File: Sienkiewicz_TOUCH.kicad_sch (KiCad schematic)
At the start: 0 parts

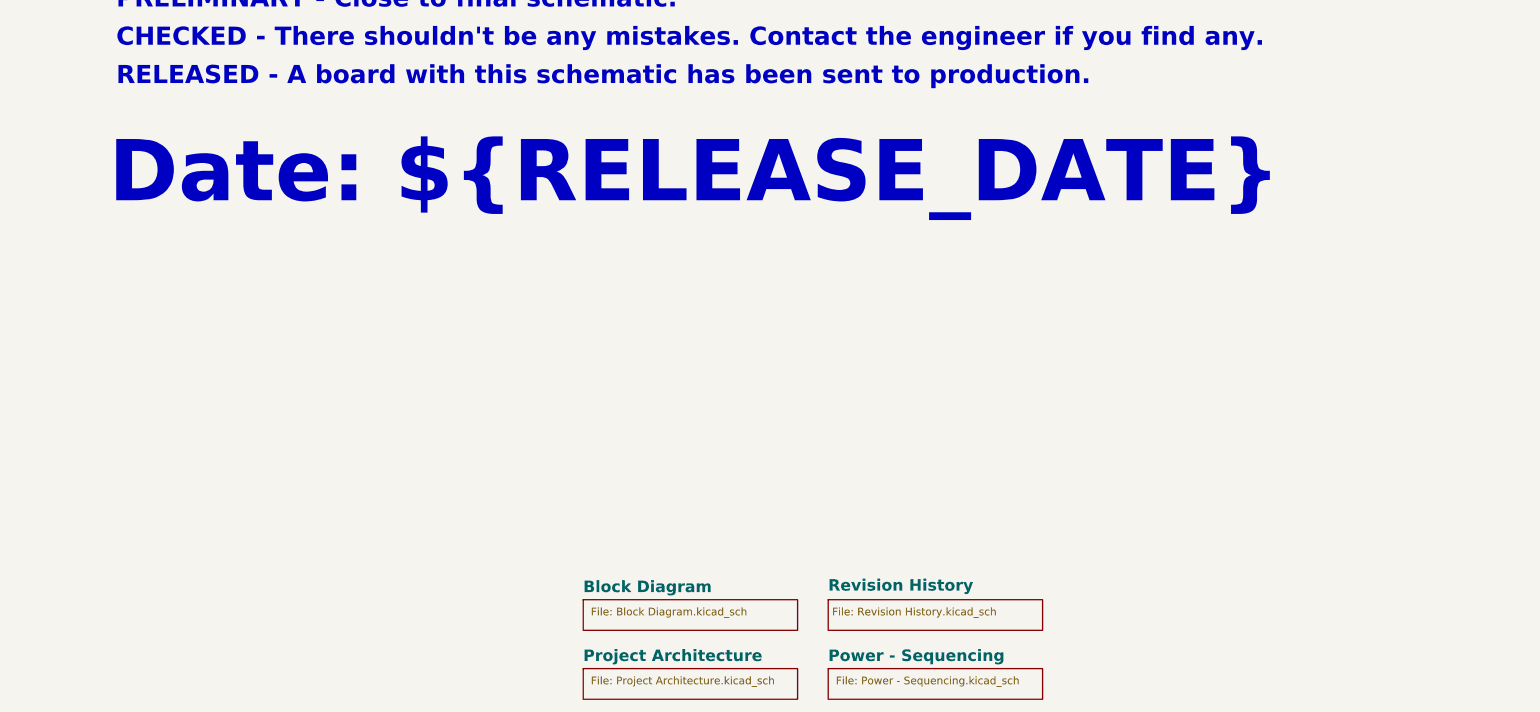
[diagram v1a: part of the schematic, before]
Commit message: documentation update / block diagram
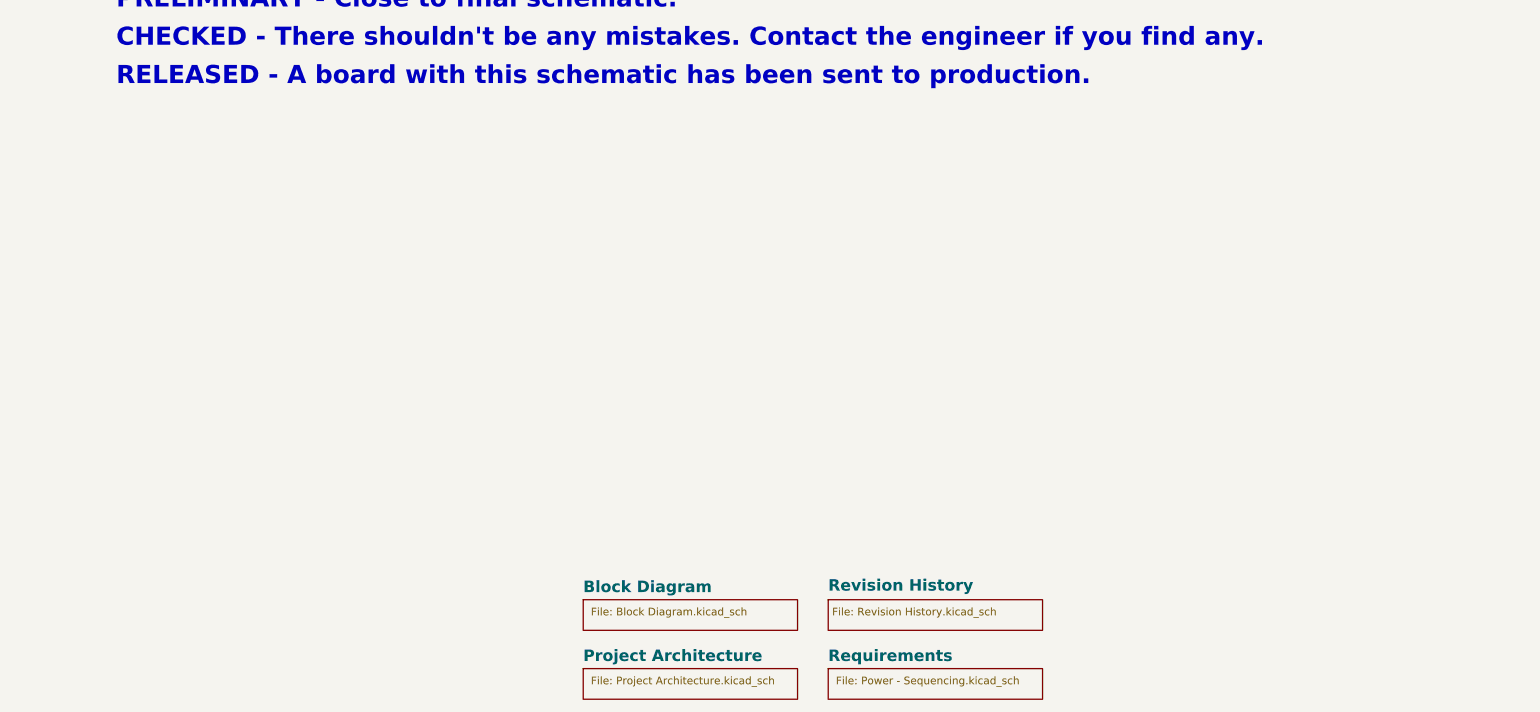
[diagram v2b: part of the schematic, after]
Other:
- sheet Power - Sequencing renamed Requirements
- note removed: "Date: ${RELEASE_DATE}"
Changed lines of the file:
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@@
-		)
-	)
-	(text "Date: ${RELEASE_DATE}"
-		(exclude_from_sim no)
-		(at 220.98 237.49 0)
-		(effects
-			(font
-				(face "Times New Roman")
-				(size 10.16 10.16)
-				(thickness 0.6)
-				(bold yes)
-				(color 200 200 200 1)
-			)
-			(justify left bottom)
 		)
 	)
@@
 			(color 0 0 0 0.0000)
 		)
-		(property "Sheetname" "Power - Sequencing"
+		(property "Sheetname" "Requirements"
 			(at 340.36 312.6609 0)
 			(effects

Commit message: documentation update /requirements /schematic
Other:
- note removed: "${SHEET_NAME_31}"
- note removed: "${SHEET_NAME_32}"
- note removed: "${SHEET_NAME_33}"
- note removed: "${SHEET_NAME_34}"
- note removed: "${SHEET_NAME_35}"
- note removed: "${SHEET_NAME_36}"
- note removed: "${SHEET_NAME_37}"
- note removed: "${SHEET_NAME_38}"
- note removed: "${SHEET_NAME_39}"
- note removed: "${SHEET_NAME_40}"
